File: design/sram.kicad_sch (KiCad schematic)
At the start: 43 parts, among them U10 IS61WV12816EDBLL-10TLI

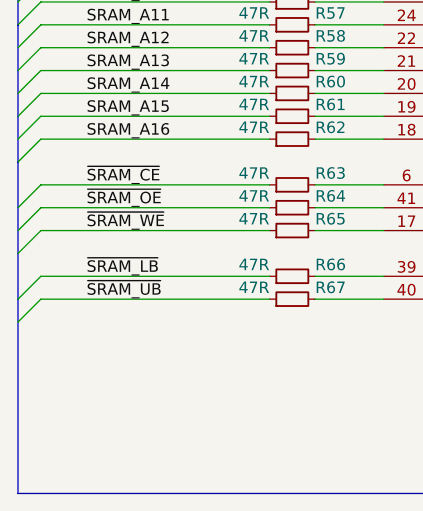
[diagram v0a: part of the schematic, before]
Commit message: Rename buses from X..0 to 0..X
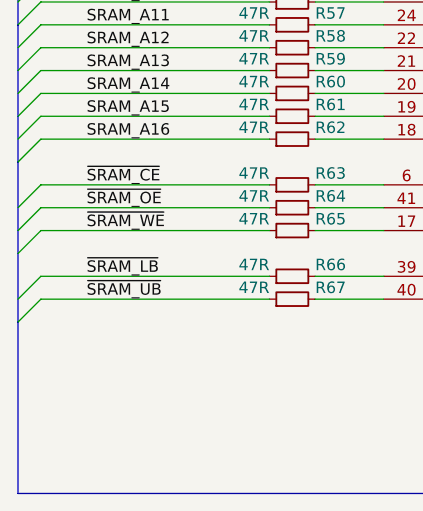
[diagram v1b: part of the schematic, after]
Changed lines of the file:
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@@
-(kicad_sch (version 20200506) (host eeschema "5.99.0-unknown-c3b50d3~101~ubuntu18.04.1")
-  (page "A4")
+(kicad_sch (version 20200512) (host eeschema "5.99.0-unknown-2cf82d9~101~ubuntu18.04.1")
+  (page 1 8)
+  (paper "A4")
   (title_block
     (title "Digitizer 10b 105 MSPS with FPGA")
@@
     (comment 2 "access time: 10 ns")
   )
-  (bus_alias "SRAM" (members "SRAM_IO[15..0]" "SRAM_A[16..0]" "~SRAM_CE" "~SRAM_OE" "~SRAM_WE" "~SRAM_LB" "~SRAM_UB"))
+  (bus_alias "SRAM" (members "SRAM_IO[0..15]" "SRAM_A[0..16]" "~SRAM_CE" "~SRAM_OE" "~SRAM_WE" "~SRAM_LB" "~SRAM_UB"))
   (junction (at 97.79 133.35))
   (junction (at 219.71 63.5))
@@
   (bus (pts (xy 36.83 96.52) (xy 36.83 101.6)))
   (bus (pts (xy 36.83 101.6) (xy 36.83 106.68)))
-  (bus (pts (xy 36.83 106.68) (xy 36.83 111.76)))
-  (bus (pts (xy 36.83 111.76) (xy 36.83 116.84)))
-  (bus (pts (xy 36.83 116.84) (xy 36.83 121.92)))
-  (bus (pts (xy 36.83 121.92) (xy 36.83 143.51)))
+  (bus (pts (xy 36.83 106.68) (xy 36.83 114.3)))
+  (bus (pts (xy 36.83 114.3) (xy 36.83 116.84)))
+  (bus (pts (xy 36.83 116.84) (xy 36.83 124.46)))
+  (bus (pts (xy 36.83 124.46) (xy 36.83 143.51)))
   (bus (pts (xy 36.83 143.51) (xy 158.75 143.51)))
   (bus (pts (xy 158.75 63.5) (xy 158.75 68.58)))

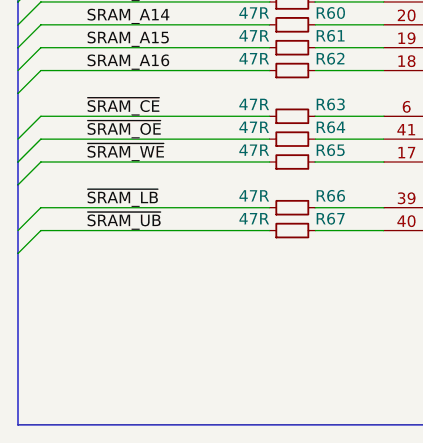
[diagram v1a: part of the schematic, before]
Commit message: Added RAM layout
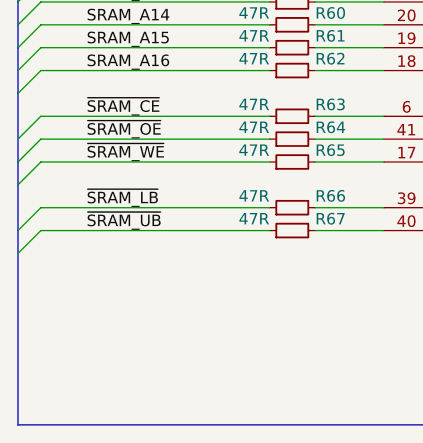
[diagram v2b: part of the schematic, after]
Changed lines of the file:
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@@
 (kicad_sch (version 20200512) (host eeschema "5.99.0-unknown-2cf82d9~101~ubuntu18.04.1")
-  (page 1 8)
+  (page 6 8)
   (paper "A4")
   (title_block
@@
   (bus (pts (xy 36.83 101.6) (xy 36.83 106.68)))
   (bus (pts (xy 36.83 106.68) (xy 36.83 114.3)))
-  (bus (pts (xy 36.83 114.3) (xy 36.83 116.84)))
-  (bus (pts (xy 36.83 116.84) (xy 36.83 124.46)))
-  (bus (pts (xy 36.83 124.46) (xy 36.83 143.51)))
+  (bus (pts (xy 36.83 114.3) (xy 36.83 121.92)))
+  (bus (pts (xy 36.83 121.92) (xy 36.83 143.51)))
   (bus (pts (xy 36.83 143.51) (xy 158.75 143.51)))
   (bus (pts (xy 158.75 63.5) (xy 158.75 68.58)))

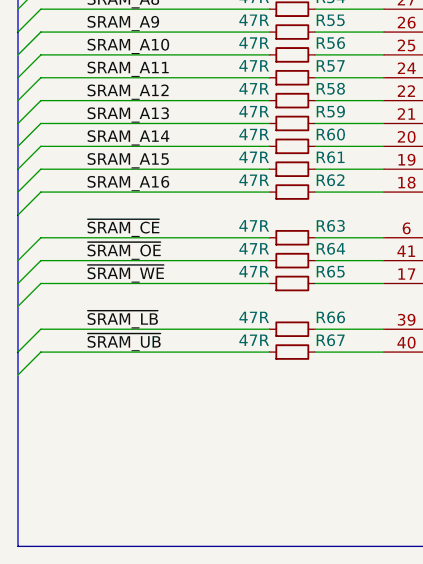
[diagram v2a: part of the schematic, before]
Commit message: Updated layout
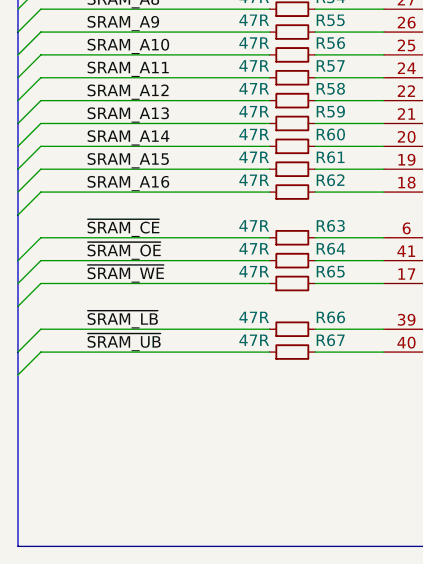
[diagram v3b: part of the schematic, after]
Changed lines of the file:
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@@
 (kicad_sch (version 20200512) (host eeschema "5.99.0-unknown-2cf82d9~101~ubuntu18.04.1")
-  (page 6 8)
+  (page 1 8)
   (paper "A4")
   (title_block
@@
   (bus (pts (xy 36.83 96.52) (xy 36.83 101.6)))
   (bus (pts (xy 36.83 101.6) (xy 36.83 106.68)))
-  (bus (pts (xy 36.83 106.68) (xy 36.83 114.3)))
-  (bus (pts (xy 36.83 114.3) (xy 36.83 121.92)))
+  (bus (pts (xy 36.83 106.68) (xy 36.83 111.76)))
+  (bus (pts (xy 36.83 111.76) (xy 36.83 116.84)))
+  (bus (pts (xy 36.83 116.84) (xy 36.83 121.92)))
   (bus (pts (xy 36.83 121.92) (xy 36.83 143.51)))
   (bus (pts (xy 36.83 143.51) (xy 158.75 143.51)))

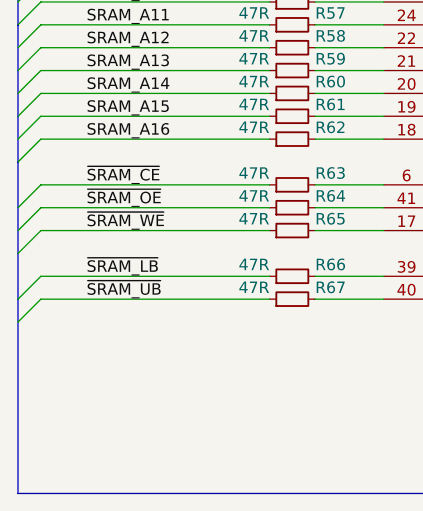
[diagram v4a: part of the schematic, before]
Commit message: Created new RAM placement and test layout
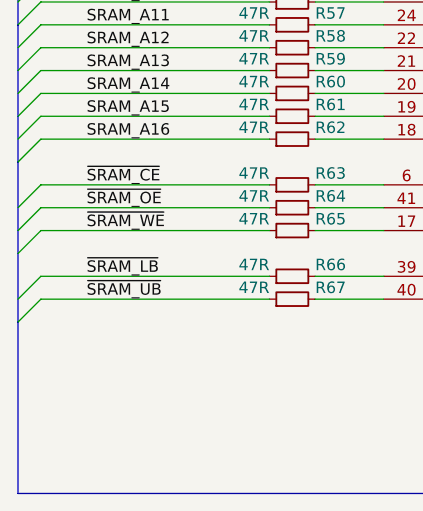
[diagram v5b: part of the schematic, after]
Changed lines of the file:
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@@
   (bus (pts (xy 36.83 96.52) (xy 36.83 101.6)))
   (bus (pts (xy 36.83 101.6) (xy 36.83 106.68)))
-  (bus (pts (xy 36.83 106.68) (xy 36.83 111.76)))
-  (bus (pts (xy 36.83 111.76) (xy 36.83 116.84)))
-  (bus (pts (xy 36.83 116.84) (xy 36.83 121.92)))
-  (bus (pts (xy 36.83 121.92) (xy 36.83 143.51)))
+  (bus (pts (xy 36.83 106.68) (xy 36.83 114.3)))
+  (bus (pts (xy 36.83 114.3) (xy 36.83 116.84)))
+  (bus (pts (xy 36.83 116.84) (xy 36.83 124.46)))
+  (bus (pts (xy 36.83 124.46) (xy 36.83 143.51)))
   (bus (pts (xy 36.83 143.51) (xy 158.75 143.51)))
   (bus (pts (xy 158.75 63.5) (xy 158.75 68.58)))

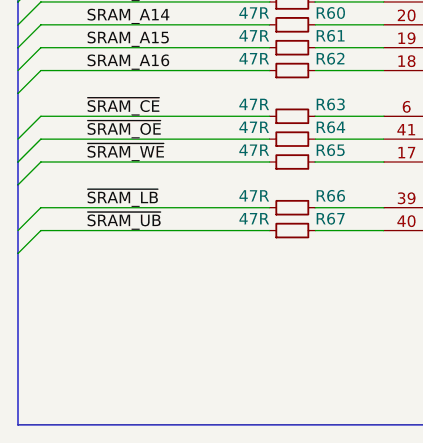
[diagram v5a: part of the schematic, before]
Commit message: Added FPGA LEDs layout
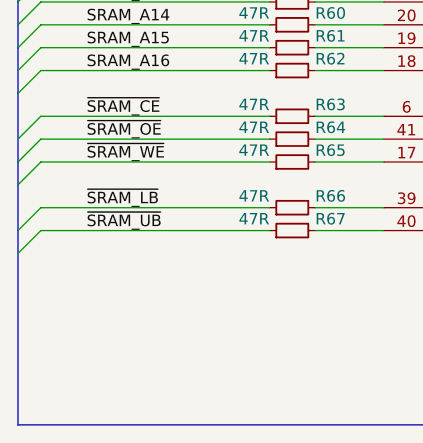
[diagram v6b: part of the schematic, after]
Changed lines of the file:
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@@
-(kicad_sch (version 20200512) (host eeschema "5.99.0-unknown-2cf82d9~101~ubuntu18.04.1")
-  (page 6 8)
+(kicad_sch (version 20200512) (host eeschema "5.99.0-unknown-ad88874~101~ubuntu18.04.1")
+  (page 1 8)
   (paper "A4")
   (title_block
@@
   (bus (pts (xy 36.83 101.6) (xy 36.83 106.68)))
   (bus (pts (xy 36.83 106.68) (xy 36.83 114.3)))
-  (bus (pts (xy 36.83 114.3) (xy 36.83 116.84)))
-  (bus (pts (xy 36.83 116.84) (xy 36.83 124.46)))
-  (bus (pts (xy 36.83 124.46) (xy 36.83 143.51)))
+  (bus (pts (xy 36.83 114.3) (xy 36.83 121.92)))
+  (bus (pts (xy 36.83 121.92) (xy 36.83 143.51)))
   (bus (pts (xy 36.83 143.51) (xy 158.75 143.51)))
   (bus (pts (xy 158.75 63.5) (xy 158.75 68.58)))

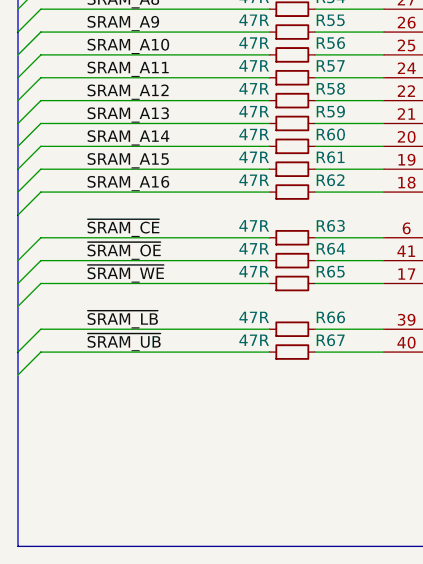
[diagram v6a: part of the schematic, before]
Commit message: Added MCU LED layout
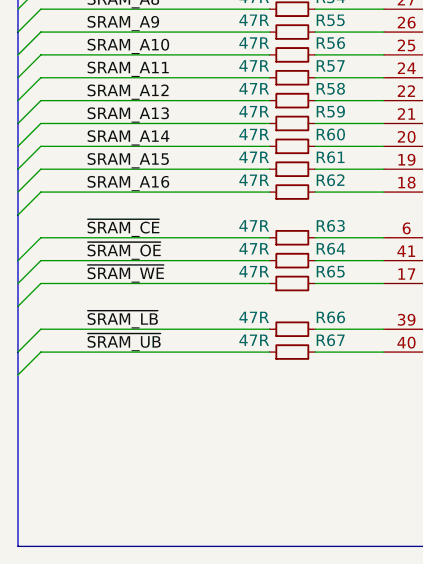
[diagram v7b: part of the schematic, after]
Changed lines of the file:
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@@
   (bus (pts (xy 36.83 96.52) (xy 36.83 101.6)))
   (bus (pts (xy 36.83 101.6) (xy 36.83 106.68)))
-  (bus (pts (xy 36.83 106.68) (xy 36.83 114.3)))
-  (bus (pts (xy 36.83 114.3) (xy 36.83 121.92)))
+  (bus (pts (xy 36.83 106.68) (xy 36.83 111.76)))
+  (bus (pts (xy 36.83 111.76) (xy 36.83 116.84)))
+  (bus (pts (xy 36.83 116.84) (xy 36.83 121.92)))
   (bus (pts (xy 36.83 121.92) (xy 36.83 143.51)))
   (bus (pts (xy 36.83 143.51) (xy 158.75 143.51)))

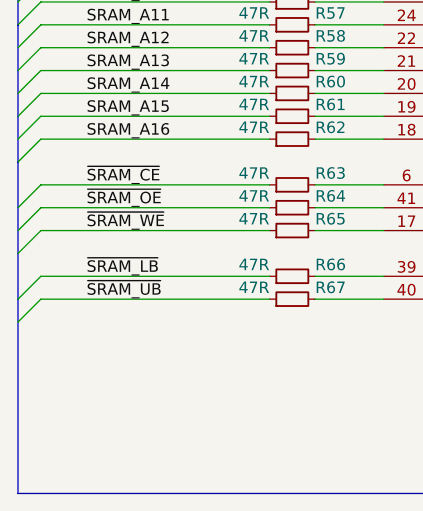
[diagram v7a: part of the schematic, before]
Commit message: Added SPI connection
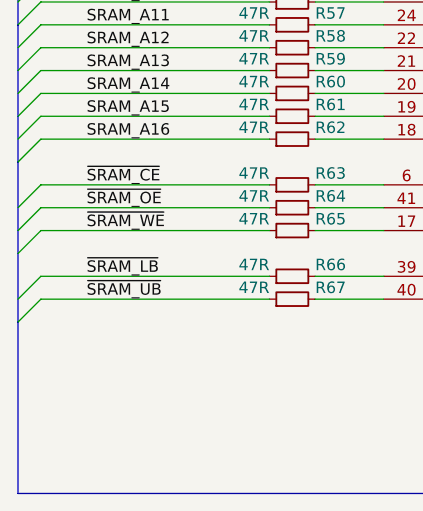
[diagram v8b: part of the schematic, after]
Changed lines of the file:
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@@
   (bus (pts (xy 36.83 96.52) (xy 36.83 101.6)))
   (bus (pts (xy 36.83 101.6) (xy 36.83 106.68)))
-  (bus (pts (xy 36.83 106.68) (xy 36.83 111.76)))
-  (bus (pts (xy 36.83 111.76) (xy 36.83 116.84)))
-  (bus (pts (xy 36.83 116.84) (xy 36.83 121.92)))
-  (bus (pts (xy 36.83 121.92) (xy 36.83 143.51)))
+  (bus (pts (xy 36.83 106.68) (xy 36.83 114.3)))
+  (bus (pts (xy 36.83 114.3) (xy 36.83 116.84)))
+  (bus (pts (xy 36.83 116.84) (xy 36.83 124.46)))
+  (bus (pts (xy 36.83 124.46) (xy 36.83 143.51)))
   (bus (pts (xy 36.83 143.51) (xy 158.75 143.51)))
   (bus (pts (xy 158.75 63.5) (xy 158.75 68.58)))
